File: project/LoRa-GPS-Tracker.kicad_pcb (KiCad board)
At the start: 2 copper layers, 38.9 x 40 mm, 60 parts, among them IC101 MCP73831-2-OT, IC102 MCP100T-300I/TT, IC103 FT230XS, IC104 NCP705MT30TCG, M101 SIM28ML, M102 RAK3172, Q101 BSS123, Q102 TP0610K, Q103 BSH205G2VL, Q104 TP0610K, SW102 ON/OFF, X101 DEBUG, X102 Conn_Coaxial, X103 BATTERY, X104 DEBUG

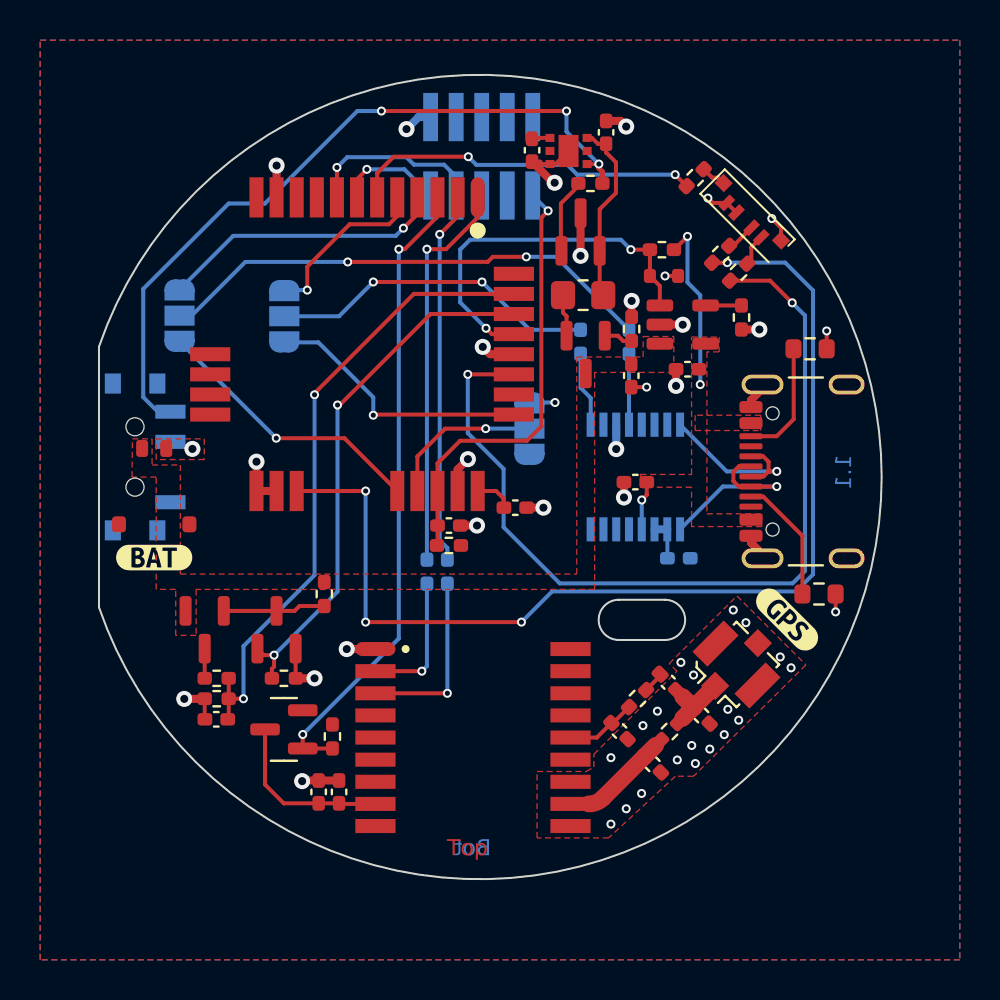
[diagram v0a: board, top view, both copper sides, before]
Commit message: Add I2C accelerometer
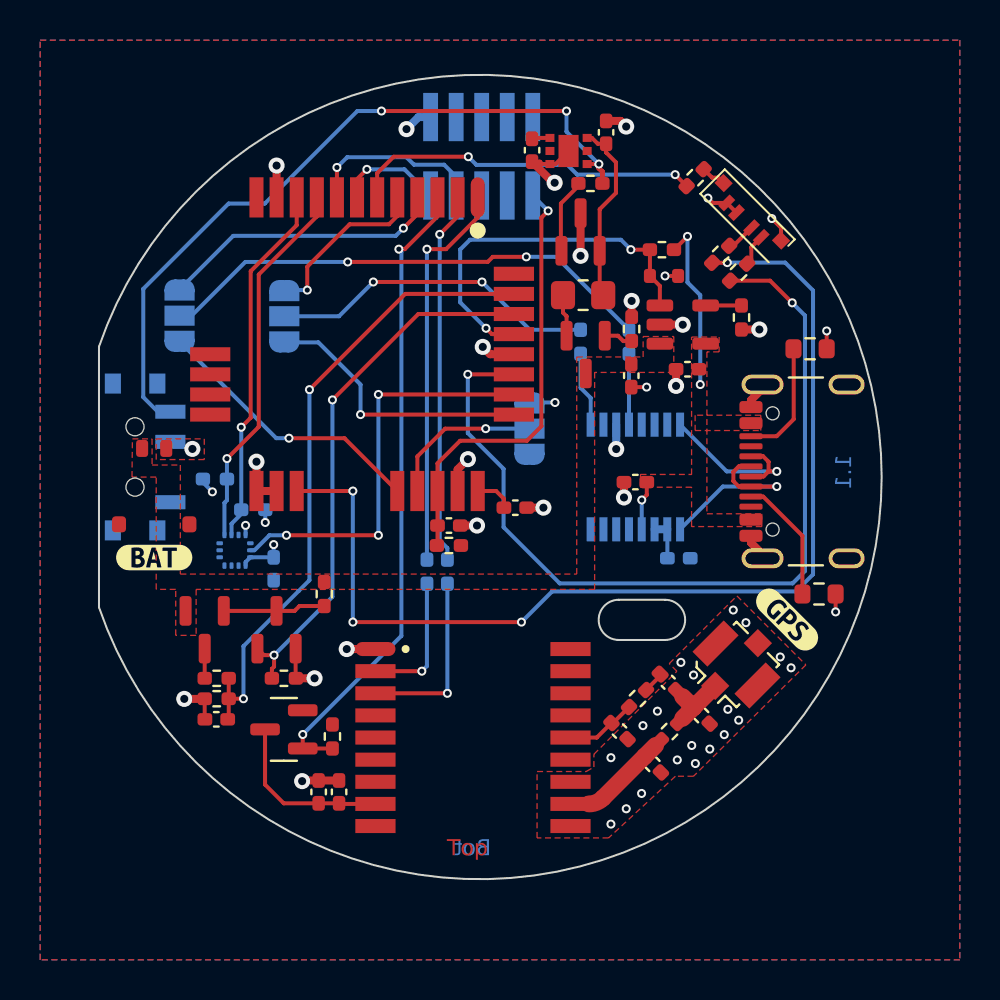
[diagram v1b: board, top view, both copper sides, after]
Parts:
- added C112: 100n, Capacitor_SMD:C_0402_1005Metric_Pad0.74x0.62mm_HandSolder, B.Cu at (134.2, 110.8)
- added IC105: LIS2DH, Package_LGA:LGA-14_2x2mm_P0.35mm_LayoutBorder3x4y, B.Cu at (132.3, 109.8)
- added R115: 3k3, Resistor_SMD:R_0402_1005Metric_Pad0.72x0.64mm_HandSolder, B.Cu at (131.3, 106.3)
- added R117: 3k3, Resistor_SMD:R_0402_1005Metric_Pad0.72x0.64mm_HandSolder, B.Cu at (133.2, 107.8)
- renumbered C104 to C103, C105 to C104, C106 to C105, C107 to C106, C108 to C107, C109 to C108, C110 to C109, C111 to C110, C112 to C111, C103 to C115, D103 to D102, Q104 to Q101, Q103 to Q102, Q101 to Q103, Q102 to Q104, R102 to R101, R103 to R102, R122 to R103, R107 to R104, R108 to R105, R109 to R106, R110 to R107, R111 to R108, R112 to R109, R113 to R110, R114 to R111, R115 to R112, R116 to R113, R117 to R114, R118 to R116, R101 to R118, R120 to R119, R119 to R120, R104 to R121, R121 to R122, R105 to R123, R106 to R124, SW102 to SW101
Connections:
- M102 pad 10: unconnected-(M102-SDA-Pad10) -> Net-(IC105-SDA/SDI)
- M102 pad 26: unconnected-(M102-ADC3-Pad26) -> /INT
- M102 pad 9: unconnected-(M102-SCL-Pad9) -> Net-(IC105-SCL/SPC)
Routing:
- net /INT: track 0.00 -> 20.4 mm, vias 0 -> 3
- net Net-(IC105-SCL/SPC): track 0.00 -> 18.7 mm, vias 0 -> 1
- net Net-(IC105-SDA/SDI): track 0.00 -> 18.1 mm, vias 0 -> 1
- net +3V0: track 6.74 -> 11.0 mm, vias 3 -> 7
